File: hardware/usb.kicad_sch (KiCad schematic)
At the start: 31 parts, among them J3 USB_C_Receptacle_USB2.0_14P, J4 USB_C_Receptacle_USB2.0_14P, J5 USB_C_Receptacle_USB2.0_14P, J6 USB_A_Stacked, U10 TPD2EUSB30, U11 TPD2EUSB30, U12 TPD2EUSB30, U13 SY6280AAC, U14 SY6280AAC, U16 TPD2EUSB30, U6 HUSB237, U7 SY6280AAC, U8 SY6280AAC, U9 TPD2EUSB30

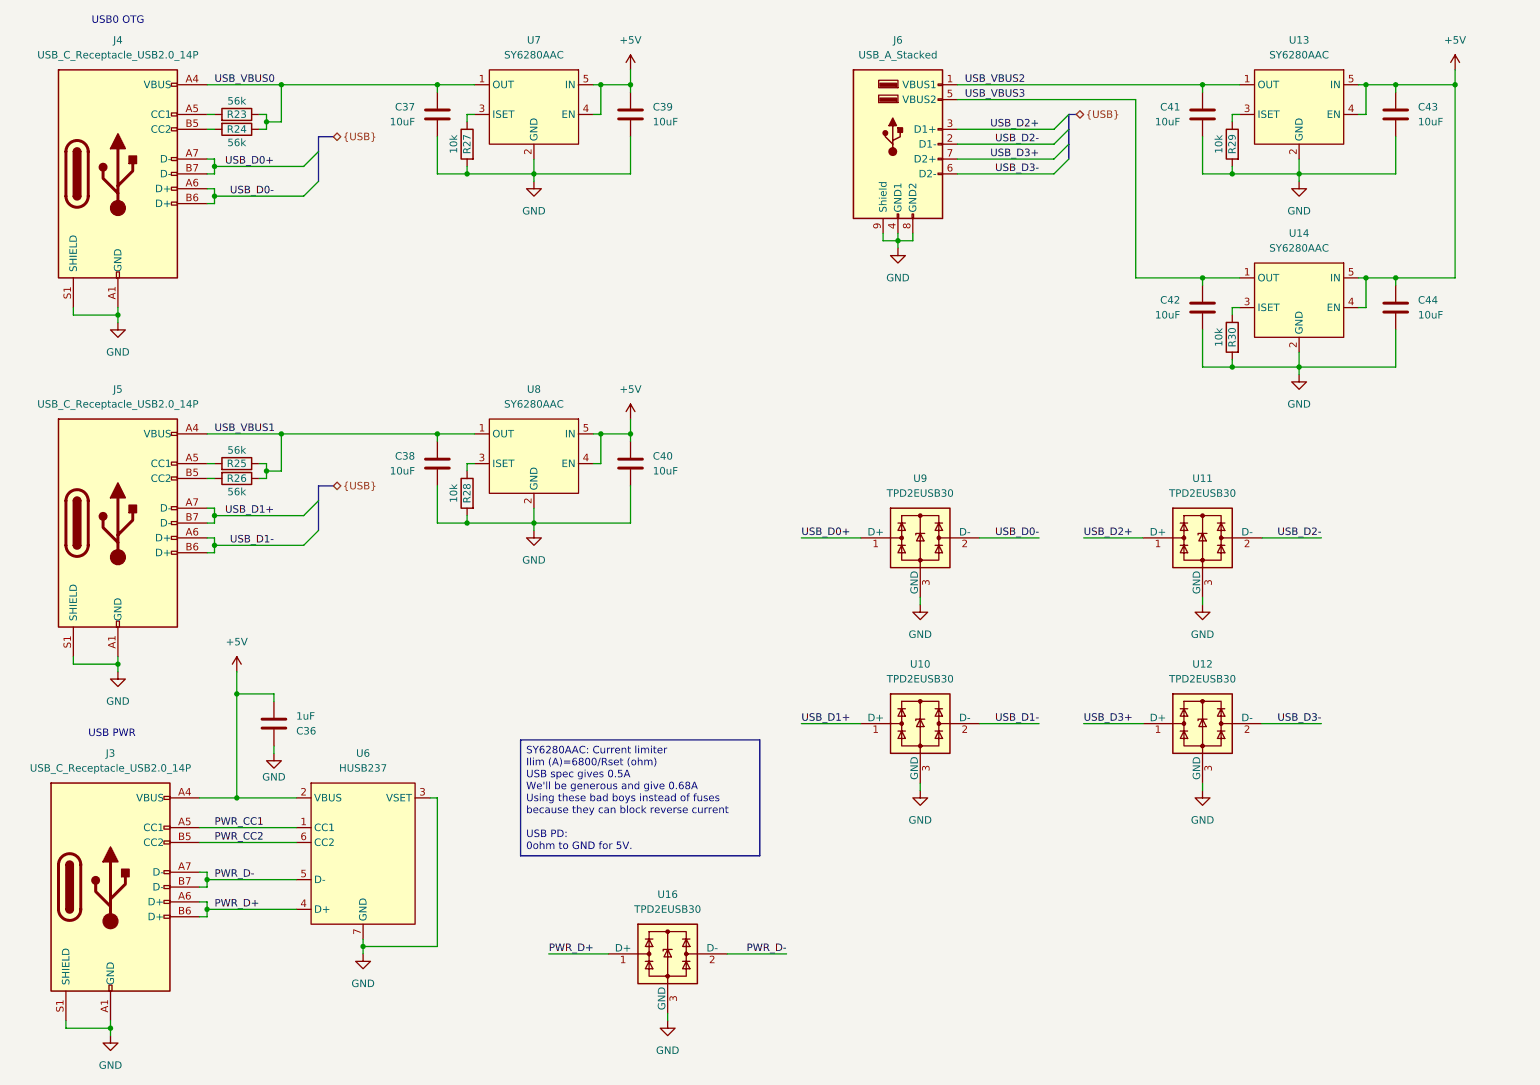
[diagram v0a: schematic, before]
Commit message: Drew most of DC DC converters
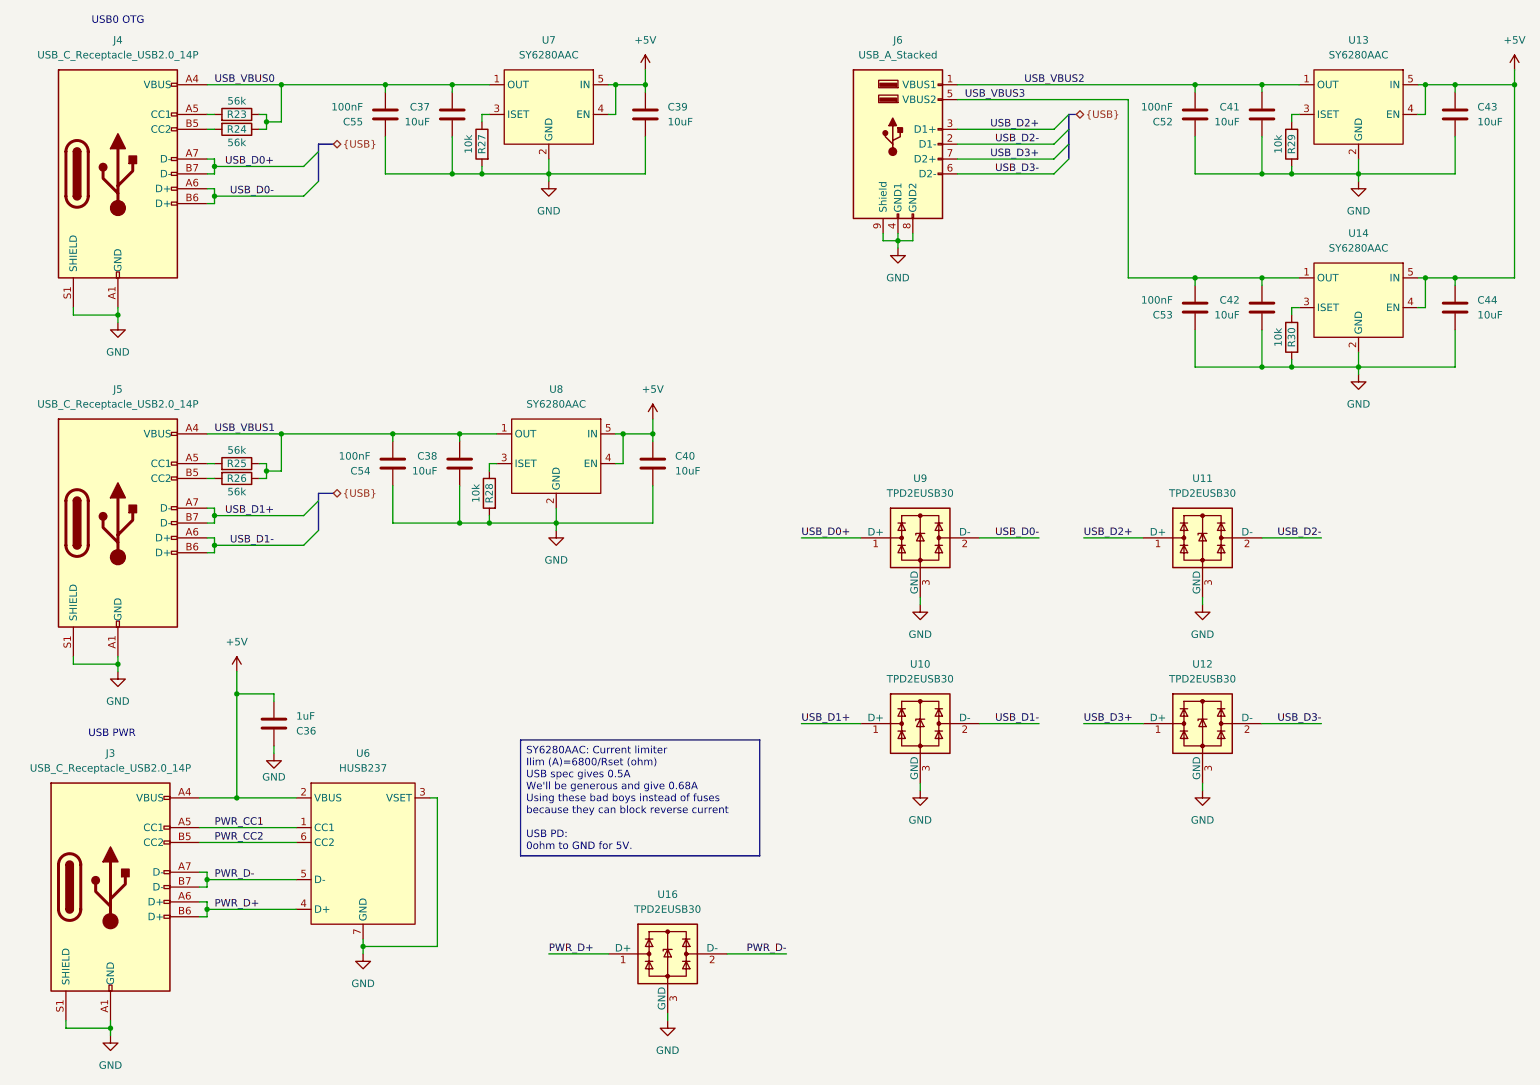
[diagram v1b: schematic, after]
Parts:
- added C52, C53, C54, C55: 100nF, Capacitor_SMD:C_0402_1005Metric, symbol Device:C
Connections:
- net GND: now also C52.1, C53.1, C54.1, C55.1
- net USB_VBUS0: now also C55.2
- net USB_VBUS1: now also C54.2
- net USB_VBUS2: now also C52.2
- net USB_VBUS3: now also C53.2
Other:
- moved on the sheet: C37, C38, C39, C40, C41, C42, C43, C44, R27, R28, R29, R30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
